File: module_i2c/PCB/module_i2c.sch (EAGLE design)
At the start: 5 parts

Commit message: fix module_i2c
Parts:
- added U$7: (no value), gclue:LOGO_GCLUE
- added U$8: (no value), gclue:LOGO_OSHW-S
- SV1, SV2, SV3, SV4, SV5: value BRICK_I2C_CONNECTOR -> (none)
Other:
- note added: "0.2"
- moved on the sheet: SV1, SV2, SV3, SV4, SV5

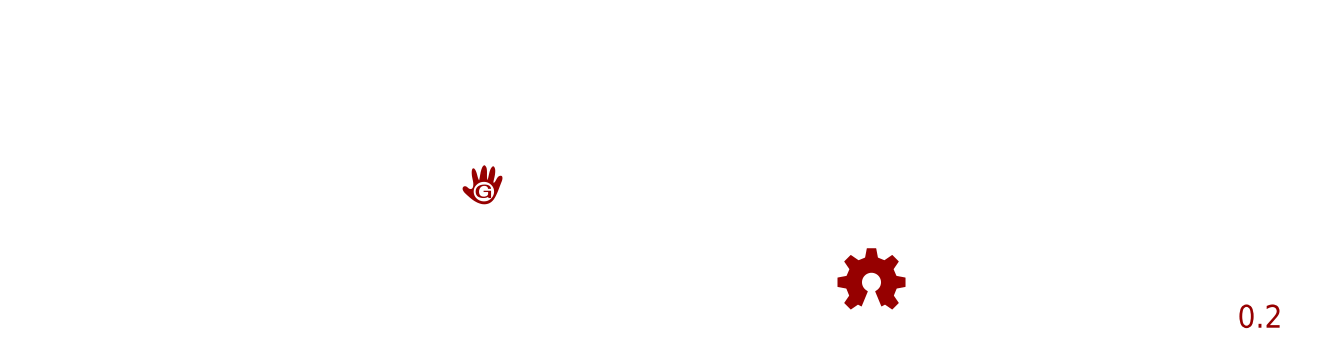
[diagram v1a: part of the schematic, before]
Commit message: Fix board size  module_i2c
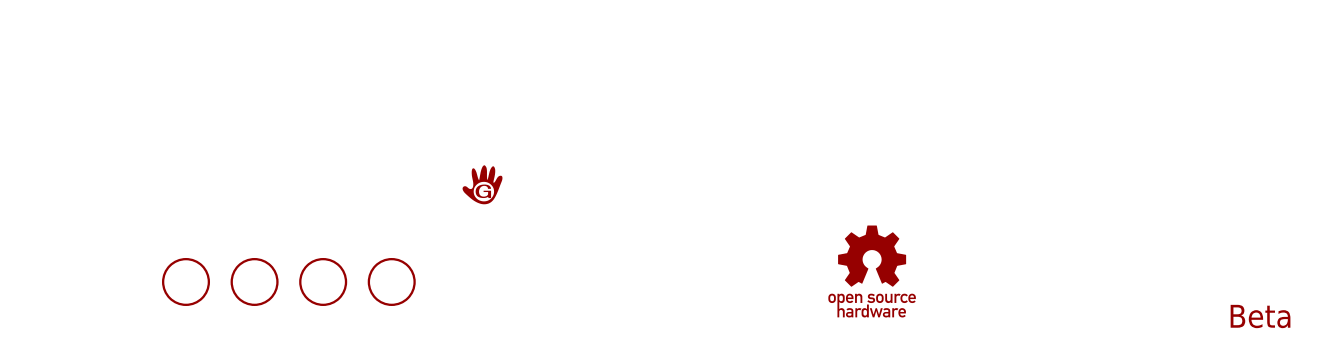
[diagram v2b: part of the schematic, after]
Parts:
- added U$10, U$9: (no value), gclue:SCREW-PAD-3MM
- added U$11: (no value), gclue:LOGO_OSHW_T-M
- added U$12: (no value), gclue:LOGO_GCLUE-M
- U$7: device gclue:LOGO_GCLUE -> gclue:SCREW-PAD-3MM
- U$8: device gclue:LOGO_OSHW-S -> gclue:SCREW-PAD-3MM
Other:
- note added: "Beta"
- note removed: "0.2"
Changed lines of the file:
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@@
 <setting verticaltext="up"/>
 </settings>
-<grid distance="0.1" unitdist="inch" unit="inch" style="lines" multiple="1" display="yes" altdistance="0.01" altunitdist="inch" altunit="inch"/>
+<grid distance="0.1" unitdist="inch" unit="inch" style="lines" multiple="1" display="no" altdistance="0.01" altunitdist="inch" altunit="inch"/>
 <layers>
 <layer number="1" name="Top" color="4" fill="1" visible="no" active="no"/>
@@
 <part name="GND5" library="gclue" deviceset="GND" device=""/>
 <part name="U$6" library="gclue" deviceset="VCC" device=""/>
-<part name="U$7" library="gclue" deviceset="LOGO_GCLUE" device=""/>
-<part name="U$8" library="gclue" deviceset="LOGO_OSHW" device="-S"/>
+<part name="U$7" library="gclue" deviceset="SCREW-PAD" device="-3MM"/>
+<part name="U$8" library="gclue" deviceset="SCREW-PAD" device="-3MM"/>
+<part name="U$9" library="gclue" deviceset="SCREW-PAD" device="-3MM"/>
+<part name="U$10" library="gclue" deviceset="SCREW-PAD" device="-3MM"/>
+<part name="U$11" library="gclue" deviceset="LOGO_OSHW_T" device="-M"/>
+<part name="U$12" library="gclue" deviceset="LOGO_GCLUE" device="-M"/>
 </parts>
 <sheets>
 <sheet>
 <plain>
-<text x="248.92" y="5.08" size="2.54" layer="94">0.2</text>
+<text x="251.46" y="5.08" size="2.54" layer="94" align="bottom-center">Beta</text>
 </plain>
 <instances>
@@
 <instance part="GND5" gate="GND" x="195.58" y="109.22"/>
 <instance part="U$6" gate="G$1" x="182.88" y="127"/>
-<instance part="U$7" gate="G$1" x="165.1" y="20.32"/>
-<instance part="U$8" gate="G$1" x="208.28" y="10.16"/>
+<instance part="U$7" gate="G$1" x="132.08" y="10.16"/>
+<instance part="U$8" gate="G$1" x="139.7" y="10.16"/>
+<instance part="U$9" gate="G$1" x="147.32" y="10.16"/>
+<instance part="U$10" gate="G$1" x="154.94" y="10.16"/>
+<instance part="U$11" gate="G$1" x="208.28" y="12.7"/>
+<instance part="U$12" gate="G$1" x="165.1" y="20.32"/>
 </instances>
 <busses>

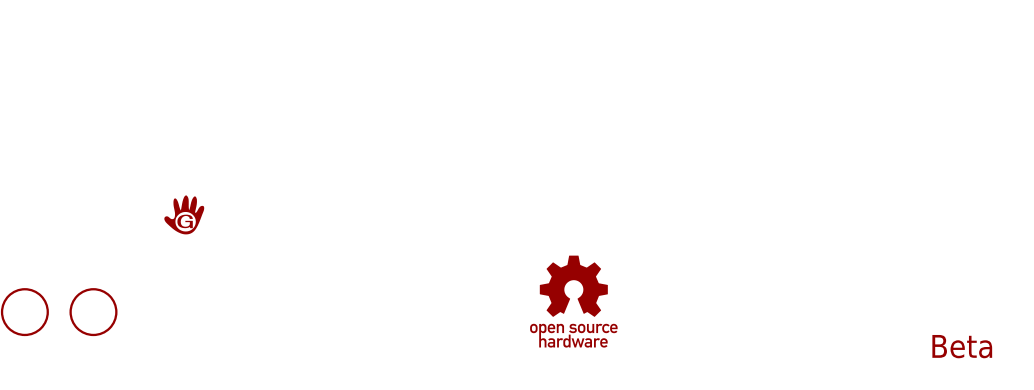
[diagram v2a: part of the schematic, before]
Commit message: refine board module_i2c
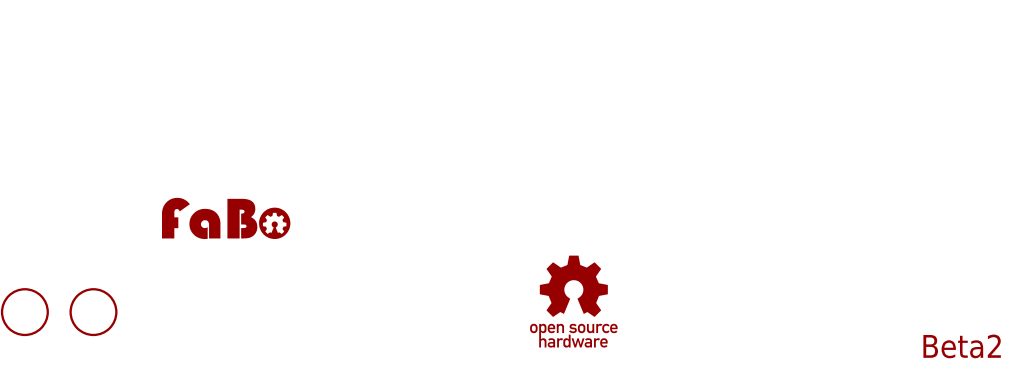
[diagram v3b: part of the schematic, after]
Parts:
- U$11: device gclue:LOGO_OSHW_T-M -> FaBo:LOGO_FABO-M
- U$12: device gclue:LOGO_GCLUE-M -> gclue:LOGO_OSHW_T-M
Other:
- note added: "Beta2"
- note removed: "Beta"
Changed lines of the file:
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@@
 <?xml version="1.0" encoding="utf-8"?>
 <!DOCTYPE eagle SYSTEM "eagle.dtd">
-<eagle version="7.2.0">
+<eagle version="7.3.0">
 <drawing>
 <settings>
@@
 <part name="U$9" library="gclue" deviceset="SCREW-PAD" device="-3MM"/>
 <part name="U$10" library="gclue" deviceset="SCREW-PAD" device="-3MM"/>
-<part name="U$11" library="gclue" deviceset="LOGO_OSHW_T" device="-M"/>
-<part name="U$12" library="gclue" deviceset="LOGO_GCLUE" device="-M"/>
+<part name="U$11" library="FaBo" deviceset="LOGO_FABO" device="-M"/>
+<part name="U$12" library="gclue" deviceset="LOGO_OSHW_T" device="-M"/>
 </parts>
 <sheets>
 <sheet>
 <plain>
-<text x="251.46" y="5.08" size="2.54" layer="94" align="bottom-center">Beta</text>
+<text x="251.46" y="5.08" size="2.54" layer="94" align="bottom-center">Beta2</text>
 </plain>
 <instances>
@@
 <instance part="U$9" gate="G$1" x="147.32" y="10.16"/>
 <instance part="U$10" gate="G$1" x="154.94" y="10.16"/>
-<instance part="U$11" gate="G$1" x="208.28" y="12.7"/>
-<instance part="U$12" gate="G$1" x="165.1" y="20.32"/>
+<instance part="U$11" gate="G$1" x="162.56" y="22.86"/>
+<instance part="U$12" gate="G$1" x="208.28" y="12.7"/>
 </instances>
 <busses>

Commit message: change revision
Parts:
- removed SV1, SV2, SV3, SV4, SV5: (no value), gclue:BRICK_I2C_CONNECTOR
- added I2C_1, I2C_2, I2C_3, I2C_4, TO_SHIELD: (no value), FaBo-Template:FABO_BRICK_I2C-CONNECTOR
- U$11: device FaBo:LOGO_FABO-M -> FaBo-etc:LOGO_OSHW-T_M
- U$12: device gclue:LOGO_OSHW_T-M -> FaBo-etc:LOGO_FABO-M
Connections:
- net GND: now also I2C_1.GND, I2C_2.GND, I2C_3.GND, I2C_4.GND, TO_SHIELD.GND; no longer SV1.GND, SV2.GND, SV3.GND, SV4.GND, SV5.GND
- net SCL: now also I2C_1.SCL, I2C_2.SCL, I2C_3.SCL, I2C_4.SCL, TO_SHIELD.SCL; no longer SV1.SCL, SV2.SCL, SV3.SCL, SV4.SCL, SV5.SCL
- net SDA: now also I2C_1.SDA, I2C_2.SDA, I2C_3.SDA, I2C_4.SDA, TO_SHIELD.SDA; no longer SV1.SDA, SV2.SDA, SV3.SDA, SV4.SDA, SV5.SDA
- net VCC: now also I2C_1.VCC, I2C_2.VCC, I2C_3.VCC, I2C_4.VCC, TO_SHIELD.VCC; no longer SV1.VCC, SV2.VCC, SV3.VCC, SV4.VCC, SV5.VCC
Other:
- note added: "1.0.0"
- note removed: "Beta2"
